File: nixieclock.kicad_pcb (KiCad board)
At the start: 2 copper layers, 146.5 x 85 mm, 69 parts, among them Q1 MMBTA42, Q2 FDS2672CT, Q3 SS8050, Q4 SS8050, U1 UCC3803, U2 K155NA1, U3 PicoW, U4 K155NA1, U5 K155NA1, U6 K155NA1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

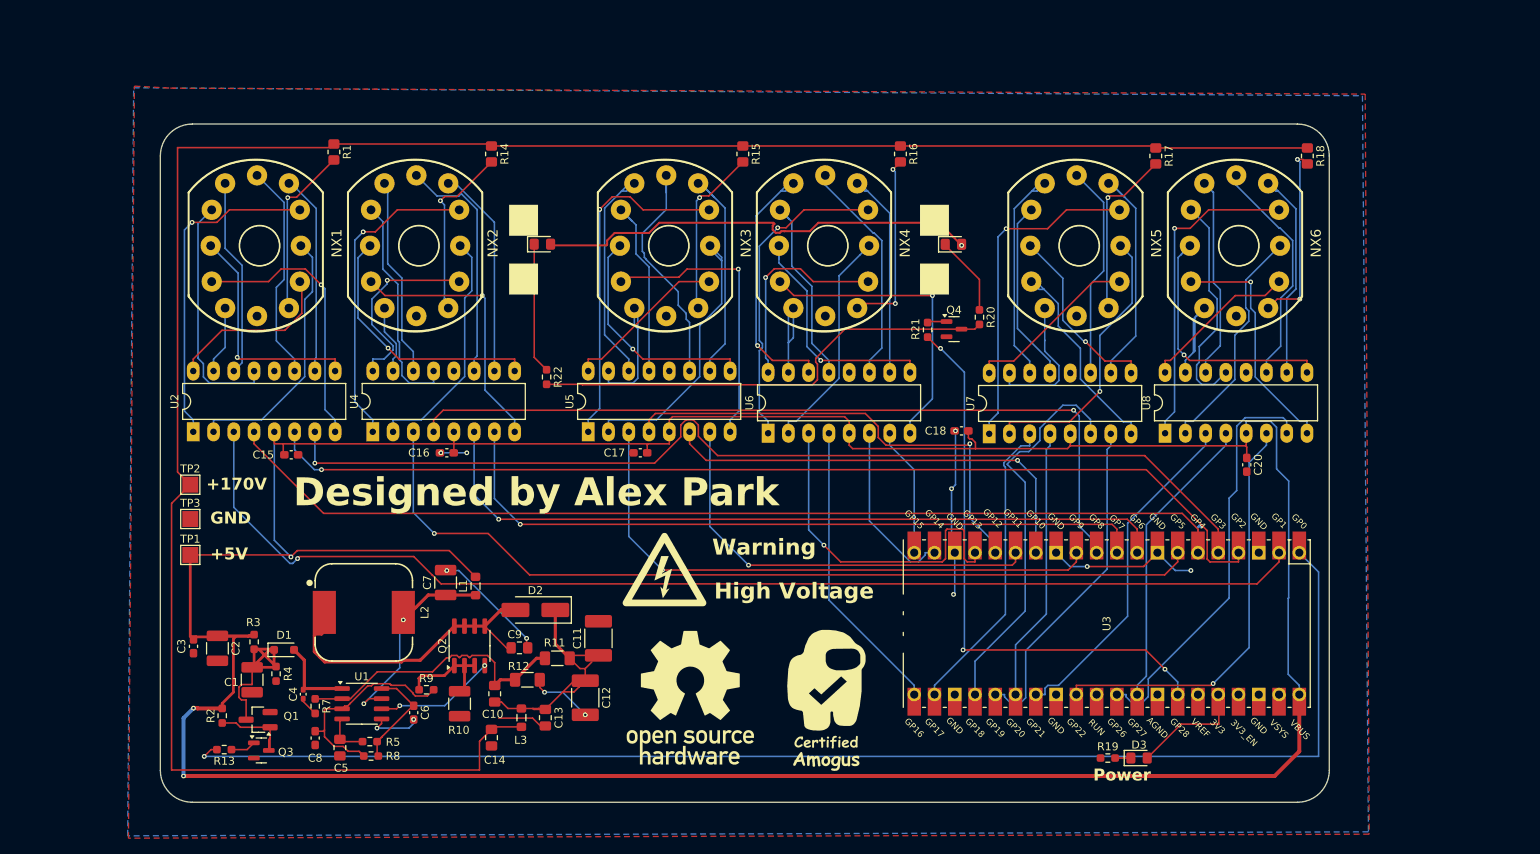
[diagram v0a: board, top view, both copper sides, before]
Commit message: Had the footprints for nixies completely wrong, redid them
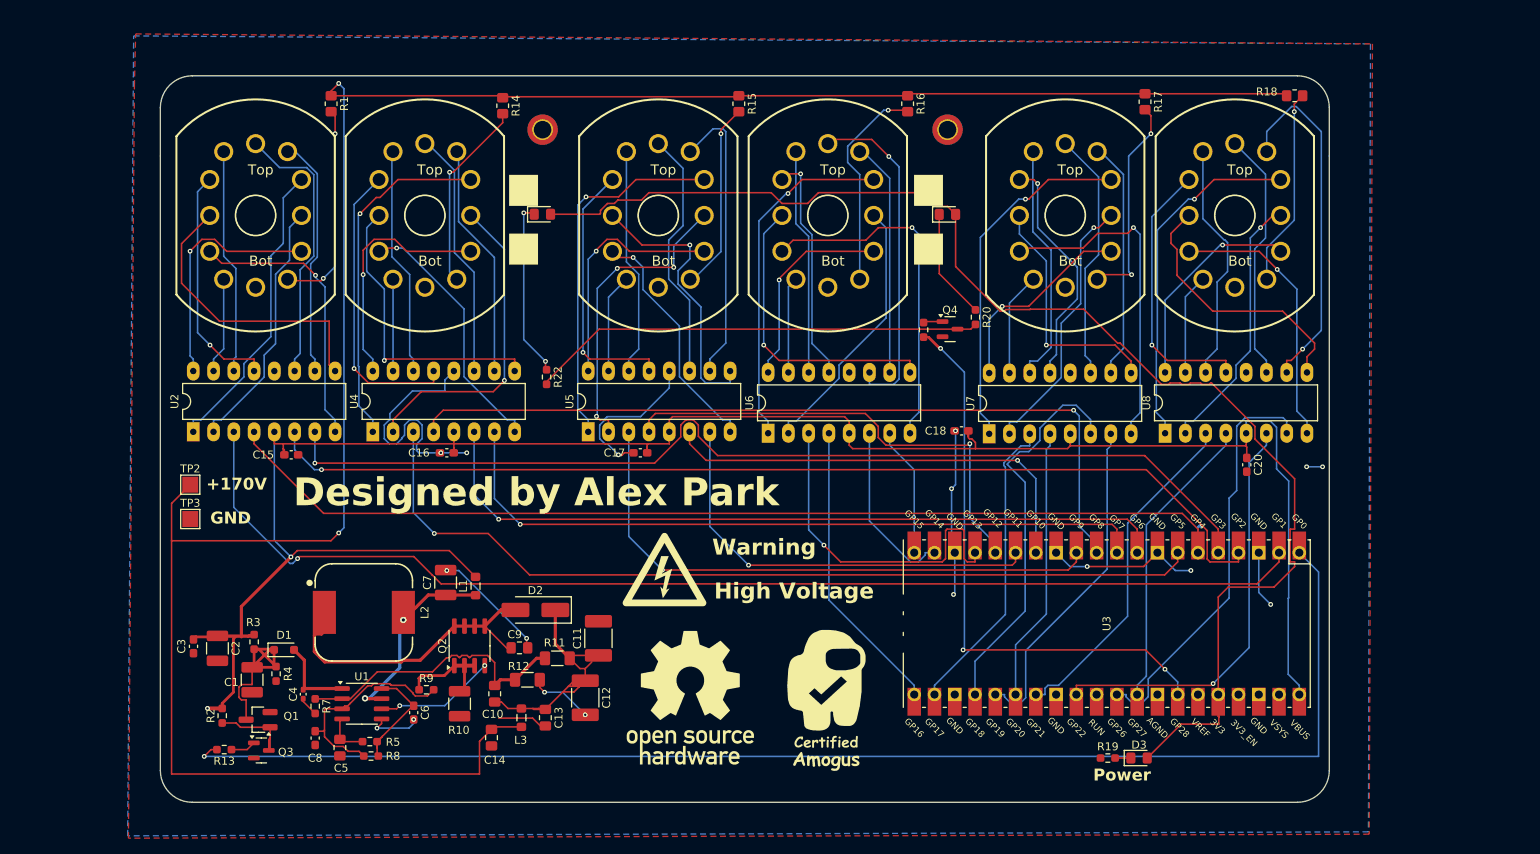
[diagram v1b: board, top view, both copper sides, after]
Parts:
- removed TP1: TestPoint_Probe, TestPoint:TestPoint_Pad_2.0x2.0mm
- added H1: M2, MountingHole:MountingHole_2.2mm_M2_DIN965_Pad_TopBottom, F.Cu at (177.2, 56.8)
- added H2: M2, MountingHole:MountingHole_2.2mm_M2_DIN965_Pad_TopBottom, F.Cu at (126.5, 56.8)
- C16: value C16 -> 0.1uF 16v
- C18: value C18 -> 0.1uF 16v
- NX1, NX2, NX3, NX4, NX5, NX6: footprint nixies-us:nixies-us-IN-12 -> nixies-us:nixies-us-IN-12-DSUB
- moved R18 7.71 mm to (220.8, 52.5), turned to 0 degrees
- moved R17 6.93 mm to (202.0, 53.2)
- moved R16 6.36 mm to (172.2, 53.5)
- moved R15 6.31 mm to (151.1, 53.5)
- moved R14 6.21 mm to (121.5, 53.8)
- moved R1 6.05 mm to (100.0, 53.5)
- moved NX5 4.18 mm to (192.0, 67.5)
- moved NX3 4.02 mm to (141.0, 67.5)
- moved NX2 3.87 mm to (111.7, 67.5)
- moved NX6 3.83 mm to (213.3, 67.5)
- moved NX1 3.83 mm to (90.5, 67.5)
- moved D5 3.82 mm to (177.2, 67.4)
- moved NX4 3.80 mm to (162.2, 67.5)
- moved D4 3.75 mm to (126.5, 67.4)
- moved Q4 0.50 mm to (177.6, 81.8)
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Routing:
- net +5V: track 433.0 -> 265.7 mm, vias 3 -> 2
- net +3V3: track 68.5 -> 166.8 mm, vias 1 -> 0
- net GND: track 77.9 -> 135.2 mm, vias 13 -> 17
- net +170V: track 268.0 -> 286.3 mm, vias 0 -> 2
- net Net-(U8-7): track 27.2 -> 44.3 mm, vias 0 -> 1
- net Net-(U7-2): track 26.6 -> 42.2 mm, vias 0 -> 1
- net Net-(U6-6): track 27.4 -> 42.7 mm, vias 0 -> 1
- net Net-(U5-4): track 22.3 -> 33.3 mm, vias 0 -> 1
- net Net-(U2-0): track 20.4 -> 30.4 mm, vias 0 -> 1
- net Net-(U5-0): track 20.7 -> 30.3 mm, vias 0 -> 1
- net Net-(U4-9): track 30.5 -> 39.9 mm, vias 0 -> 1
- net Net-(U4-4): track 28.2 -> 37.2 mm, vias 0 -> 1
- net Net-(U5-7): track 28.1 -> 36.6 mm
- net Net-(U6-3): track 29.8 -> 37.8 mm
- net Net-(U2-3): track 29.3 -> 37.0 mm, vias 1 -> 0
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- added copper zone on B.Cu, net +5V
- removed copper zone on B.Cu, net +3V3
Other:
- board size 146.5 x 85 mm -> 146.5 x 91 mm
- board text removed: "+5V"

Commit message: added clearances for safety on hv nets
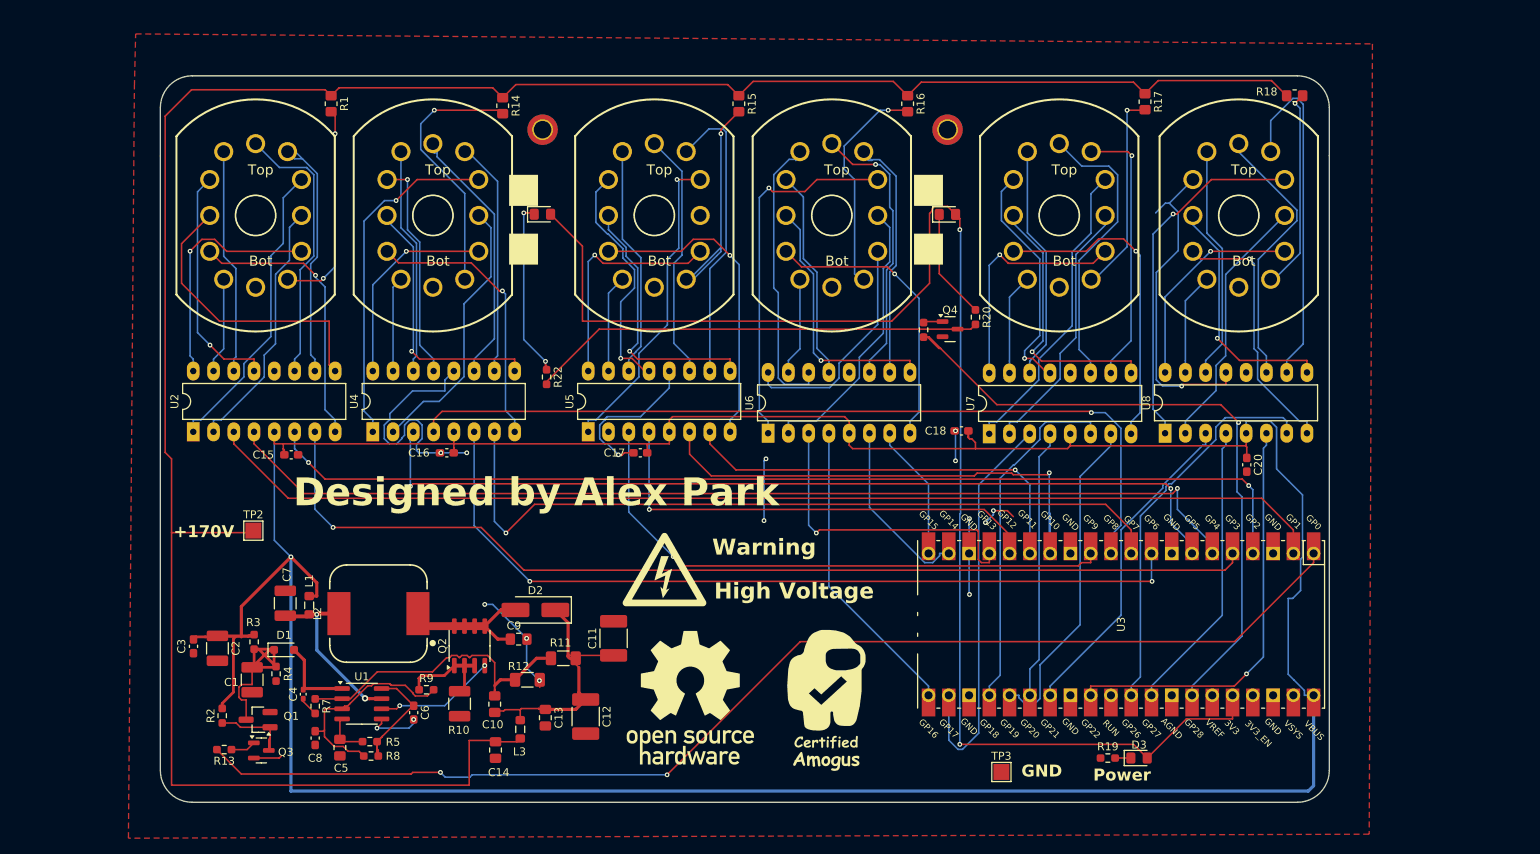
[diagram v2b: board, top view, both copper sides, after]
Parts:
- moved TP3 106.5 mm to (184.0, 137.2)
- moved L1 21.0 mm to (97.2, 116.3)
- moved C7 20.3 mm to (94.2, 116.1)
- moved TP2 9.78 mm to (90.2, 107.0)
- moved C12 2.36 mm to (131.9, 130.3)
- moved C11 1.90 mm to (135.4, 120.5)
- moved L2 1.83 mm to (105.9, 117.4), turned to 90 degrees
- moved U3 1.80 mm to (199.0, 118.8)
- moved C14 1.64 mm to (120.6, 134.5)
- moved L3 1.46 mm to (123.7, 131.9)
- moved C10 1.31 mm to (120.5, 128.8)
- moved C9 1.10 mm to (123.5, 120.6)
- moved NX2 1.00 mm to (112.8, 67.5)
- moved R11 0.75 mm to (129.1, 123.0)
- moved NX5 0.75 mm to (191.3, 67.5)
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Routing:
- net +5V: track 265.7 -> 418.2 mm, vias 2 -> 1
- net Net-(U5-9): track 38.0 -> 0.00 mm, vias 3 -> 0
- net GND: track 135.2 -> 101.8 mm, vias 17 -> 16
- net Net-(D2-A): track 38.8 -> 17.6 mm
- net GPIO0: track 168.1 -> 151.3 mm, vias 1 -> 2
- net +3V3: track 166.8 -> 181.5 mm, vias 0 -> 2
- net GPIO17: track 38.4 -> 50.9 mm
- net Net-(U5-2): track 30.3 -> 39.7 mm
- net Net-(U4-4): track 37.2 -> 27.9 mm
- net GPIO28: track 74.2 -> 83.2 mm, vias 3 -> 1
- net Net-(NX2-PadA): track 24.1 -> 32.9 mm
- net GPIO10: track 56.0 -> 64.5 mm
- net Net-(U6-5): track 28.3 -> 36.5 mm
- net Net-(U6-2): track 44.1 -> 36.5 mm
- net Net-(U6-6): track 42.7 -> 35.1 mm
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- removed copper zone on B.Cu, net +5V

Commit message: add tvs diodes for protection
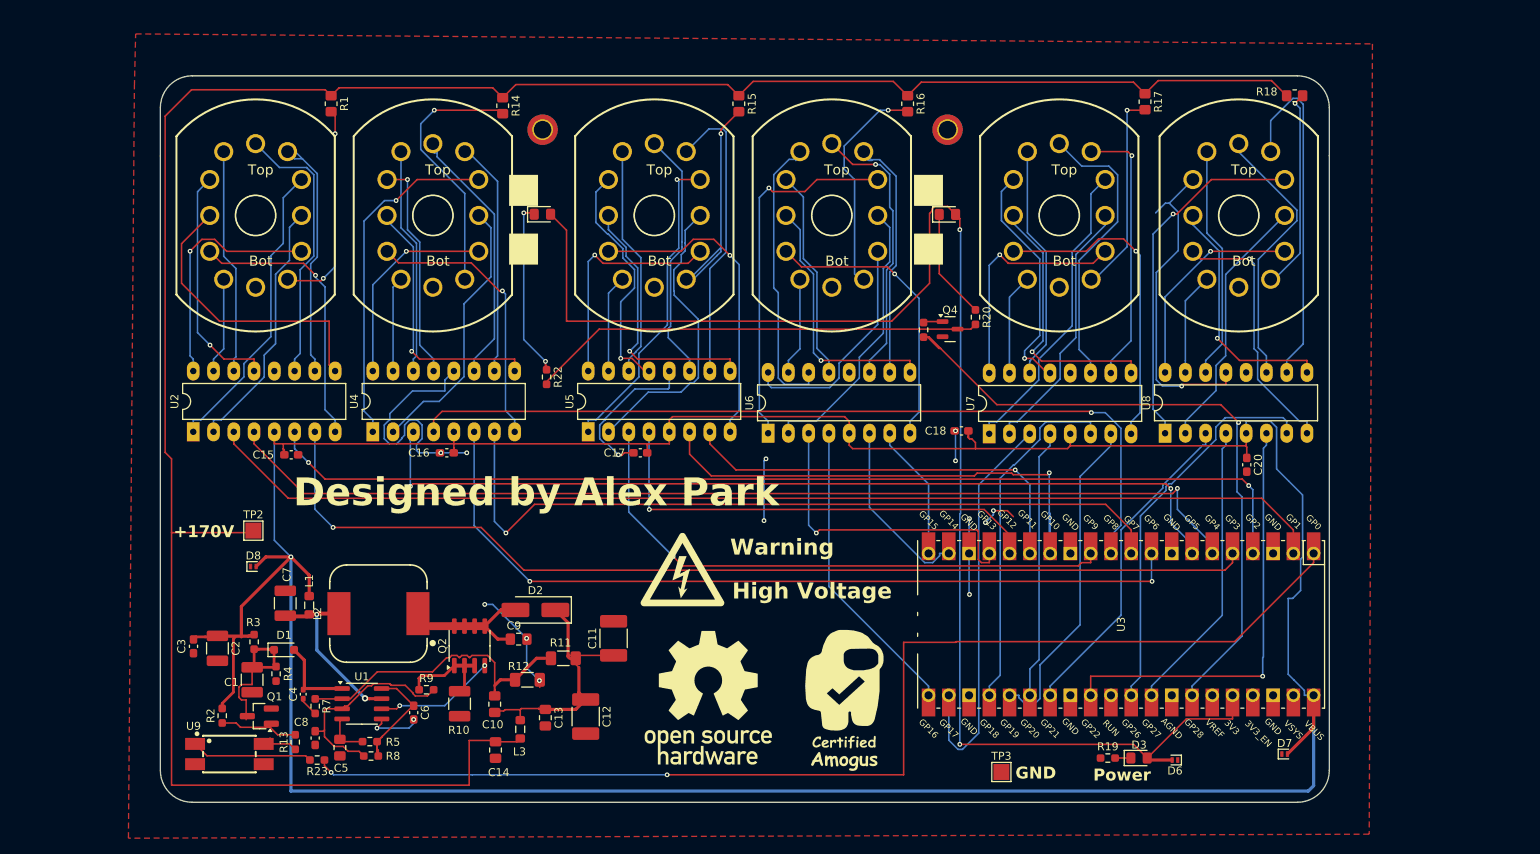
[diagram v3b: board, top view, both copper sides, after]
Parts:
- removed Q3: SS8050, Package_TO_SOT_SMD:SOT-23
- added D6: PESD5V5C1BLYL, Diode_SMD:D_SOD-882, F.Cu at (205.8, 135.8)
- added D7: PESD5V5C1BLYL, Diode_SMD:D_SOD-882, F.Cu at (219.5, 135.0)
- added D8: PESD5V5C1BLYL, Diode_SMD:D_SOD-882, F.Cu at (90.2, 111.5)
- added R23: 330, Resistor_SMD:R_0603_1608Metric_Pad0.98x0.95mm_HandSolder, F.Cu at (98.2, 135.8)
- added U9: EL817S1(C)(TU)-F, easyeda2kicad:OPTO-SMD-4_L4.6-W6.5-P2.54-LS10.3-TL, F.Cu at (87.2, 135.0)
- D4, D5: value LED_Filled -> RED
- moved R13 8.95 mm to (95.5, 133.5), turned to 90 degrees
- moved Q1 0.47 mm to (91.0, 130.2)
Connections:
- R13 pad 2: GPIO0 -> Net-(Q1-B)
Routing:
- net Net-(U5-9): track 0.00 -> 37.1 mm
- net Net-(U9-AN): track 0.00 -> 15.2 mm
- net +5V: track 418.2 -> 430.4 mm
- net Net-(D1-K): track 24.8 -> 18.6 mm
- net +3V3: track 181.5 -> 185.9 mm
- net GPIO0: track 151.3 -> 147.0 mm
- net GND: track 101.8 -> 98.3 mm
- net Net-(U9-COL): track 3.15 -> 5.83 mm
- net GPIO22: track 52.5 -> 54.6 mm
- net Net-(U5-6): track 31.2 -> 31.8 mm

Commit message: increase board size
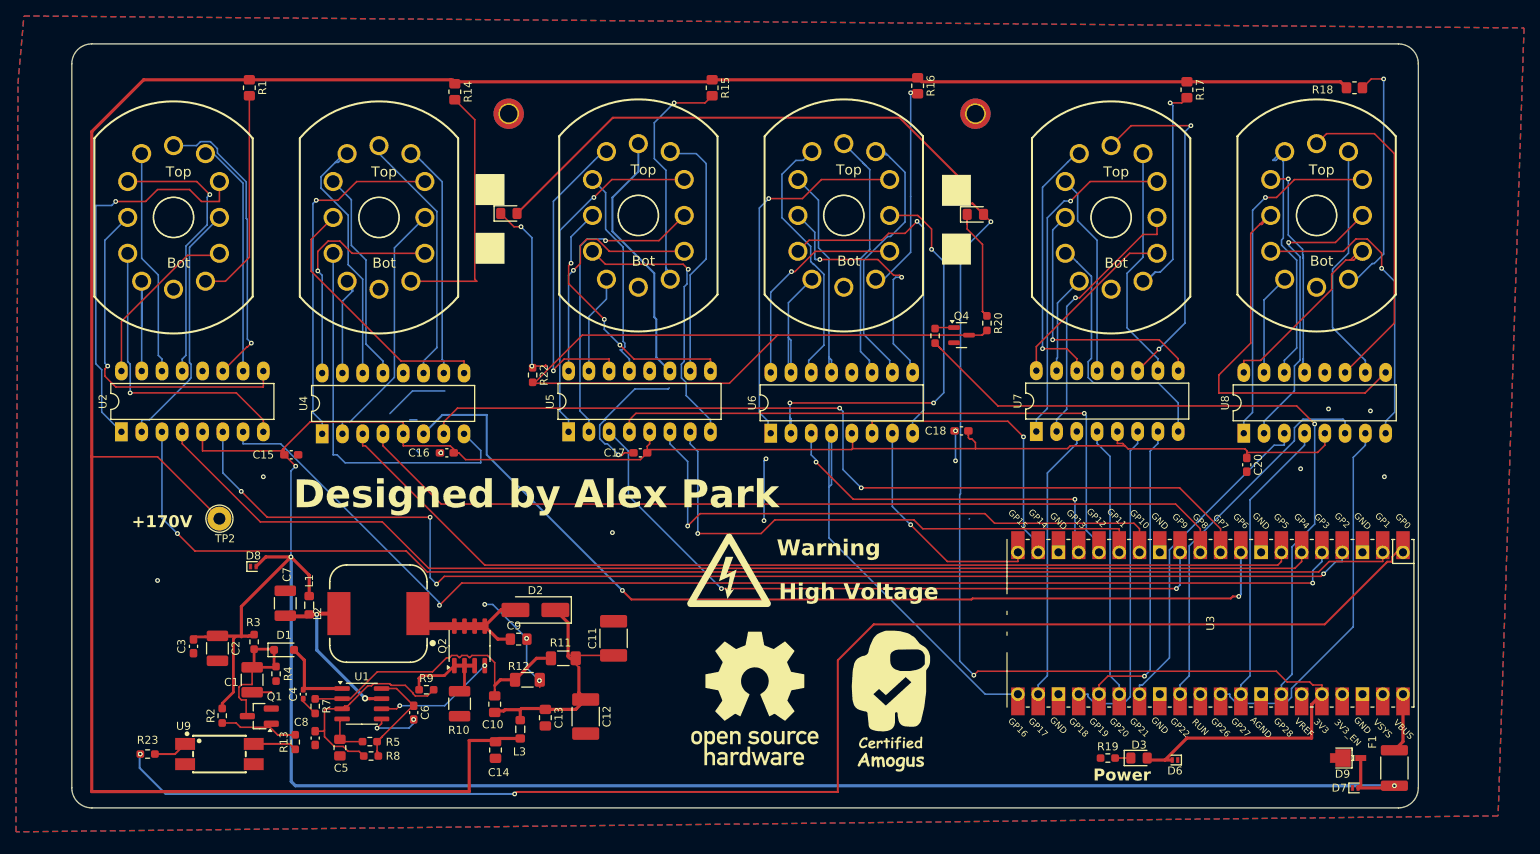
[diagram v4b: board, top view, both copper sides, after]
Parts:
- removed TP3: TestPoint_Probe, TestPoint:TestPoint_Pad_2.0x2.0mm
- added D9: SM2T3V3A, easyeda2kicad:DO-216AA_L1.9-W1.9-LS3.8-FD, F.Cu at (227.8, 135.5)
- added F1: 1.1A/2.2A, Fuse:Fuse_1812_4532Metric_Pad1.30x3.40mm_HandSolder, F.Cu at (233.2, 136.8)
- TP2: footprint TestPoint:TestPoint_Pad_2.0x2.0mm -> TestPoint:TestPoint_Loop_D2.54mm_Drill1.5mm_Beaded
- moved R23 21.3 mm to (77.0, 135.0), turned to 0 degrees
- moved U3 11.2 mm to (210.2, 118.6)
- moved R1 10.4 mm to (89.8, 51.5)
- moved NX1 10.3 mm to (80.2, 67.7)
- moved U8 9.86 mm to (214.4, 94.8)
- moved D7 9.82 mm to (228.3, 139.2)
- moved NX6 9.75 mm to (223.5, 67.5)
- moved U2 9.00 mm to (73.7, 94.6)
- moved R18 7.57 mm to (228.2, 51.5)
- moved NX2 6.76 mm to (106.0, 67.8)
- moved NX5 6.50 mm to (197.8, 67.7)
- moved U4 6.35 mm to (98.9, 94.9)
- moved R14 6.25 mm to (115.5, 52.0)
- moved U7 5.91 mm to (188.4, 94.6)
- moved R17 5.46 mm to (207.2, 51.8)
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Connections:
- U3 pad 40: +5V -> Net-(U3-VBUS)
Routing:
- net GPIO0: track 147.0 -> 184.0 mm
- net GND: track 98.3 -> 62.0 mm, vias 16 -> 19
- net Net-(Q4-C): track 57.0 -> 92.8 mm
- net +5V: track 430.4 -> 398.2 mm, vias 1 -> 3
- net +170V: track 292.8 -> 321.0 mm
- net GPIO1: track 141.7 -> 168.3 mm, vias 0 -> 1
- net GPIO2: track 132.3 -> 158.0 mm, vias 2 -> 4
- net GPIO3: track 129.4 -> 149.6 mm, vias 1 -> 2
- net GPIO4: track 130.1 -> 149.8 mm, vias 1 -> 0
- net +3V3: track 185.9 -> 204.5 mm
- net GPIO12: track 58.5 -> 77.0 mm
- net GPIO6: track 103.1 -> 121.5 mm
- net Net-(U8-3): track 30.7 -> 48.7 mm, vias 1 -> 0
- net GPIO11: track 52.4 -> 70.1 mm
- net Net-(U6-9): track 35.2 -> 52.6 mm, vias 0 -> 3
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- added copper zone on B.Cu, net GND
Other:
- board size 146.5 x 91 mm -> 168.8 x 95.8 mm
- board text removed: "GND"

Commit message: final order
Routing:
- net Net-(Q4-C): track 92.8 -> 60.2 mm
- net Net-(NX2-PadA): track 32.1 -> 29.7 mm
- net Net-(D4-K): track 23.3 -> 21.3 mm
- net Net-(U6-9): track 52.6 -> 50.6 mm
- net Net-(NX4-PadA): track 27.3 -> 25.5 mm
- net Net-(NX6-PadA): track 29.8 -> 28.1 mm
- net Net-(U7-2): track 33.1 -> 33.9 mm
- net Net-(U7-5): track 32.5 -> 33.0 mm
